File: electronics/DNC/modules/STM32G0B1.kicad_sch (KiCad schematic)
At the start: 39 parts

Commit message: Se reemplazó la hoja del IMU por la de sensores y se agregó la hoja de indicadores
- Nueva hoja Sensores: IMU BMI270 (SPI1) y barómetro BMP581 (I2C1 propio, jumper BARO_ADDR).
- Nueva hoja Indicadores: buzzer piezo CPT-12123 con FDV303N y LEDs de estado en PB4/PB5.
- Se eliminó la hoja IMU.
- MicroSD por SDIO de 4 bits con filtro TPD6F002 y TVS ESD5Z3.3 en VDD.
- PMS: AP2112K en 3V3_SYS y LP5907 + ferrita en 3V3_SEN.
- Motores movidos a PA0-PA3 (TIM5) para liberar el SDIO.
- Arquitectura.drawio actualizado a la arquitectura v1 (ELRS por UART, sin OLED).
- Se agregó docs/RESUMEN_PROYECTO_DNC.md con decisiones y pendientes.

Co-Authored-By: Claude Opus 5.5 <noreply@anthropic.com>
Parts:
- U? (x2): Category Integrated Circuits (ICs) -> (none); DK_Datasheet_Link http://www.ti.com/general/docs/suppproductinfo.tsp?distId=1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 -> (none); DK_Detail_Page /product-detail/en/texas-instruments/LM358DR/296-1014-1-ND/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 -> (none); Digi-Key_PN 296-1014-1-ND -> (none); Family Linear - Amplifiers - Instrumentation, OP Amps, Buffer Amps -> (none); MPN LM358DR -> (none); Status Active -> (none)
- U?: PROVIDER Digikey -> (none); Price 5.31 -> (none)
- U?: Category Integrated Circuits (ICs) -> (none); DK_Datasheet_Link http://www.microchip.com/mymicrochip/filehandler.aspx?ddocn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 -> (none); DK_Detail_Page /product-detail/en/microchip-technology/ATMEGA328P-AU/ATMEG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 -> (none); Digi-Key_PN ATMEGA328P-AU-ND -> (none); Family Embedded - Microcontrollers -> (none); MPN ATMEGA328P-AU -> (none); Status Active -> (none)

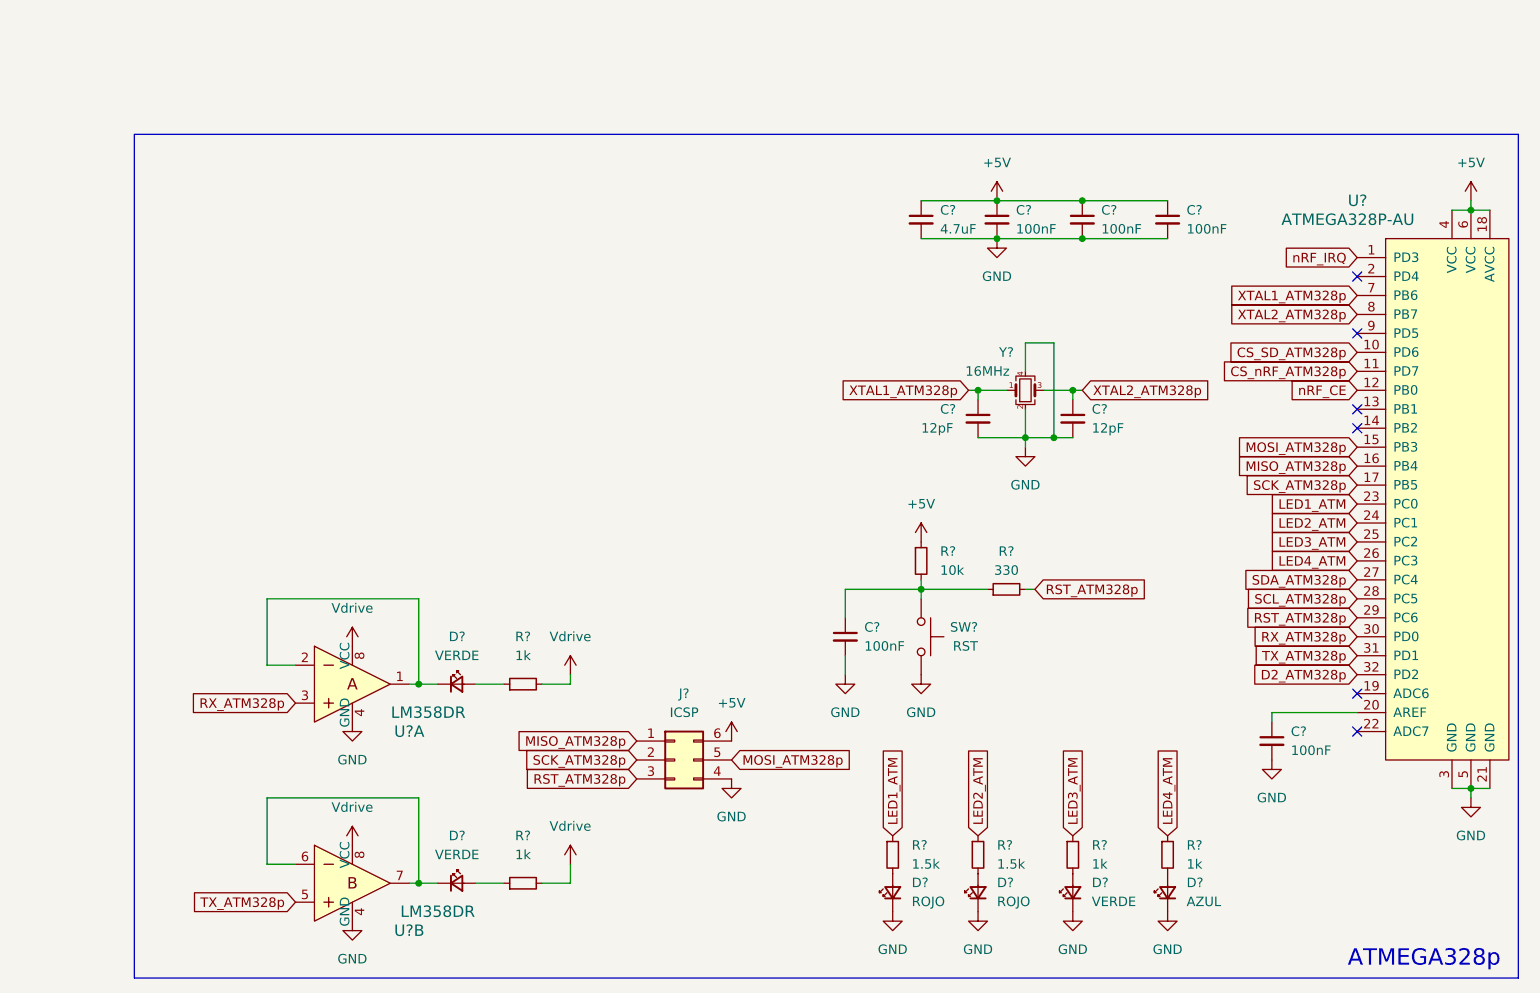
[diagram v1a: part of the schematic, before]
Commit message: Limpieza de la hoja STM32G0B1
Se eliminaron los restos del diseño anterior: ATmega328P, conector ICSP, pulsador de reset y
su cristal, LM358 y LEDs de TX/RX (alimentados desde VBUS), y los símbolos +5V y Vdrive.
La hoja ya no depende de las librerías dk_* / digikey. Quedan el STM32G0B1RETx (todavía sin
conectar) y sus dos osciladores (8 MHz y 32.768 kHz) con resistencias de 0 ohm en serie.

Co-Authored-By: Claude Opus 5.5 <noreply@anthropic.com>
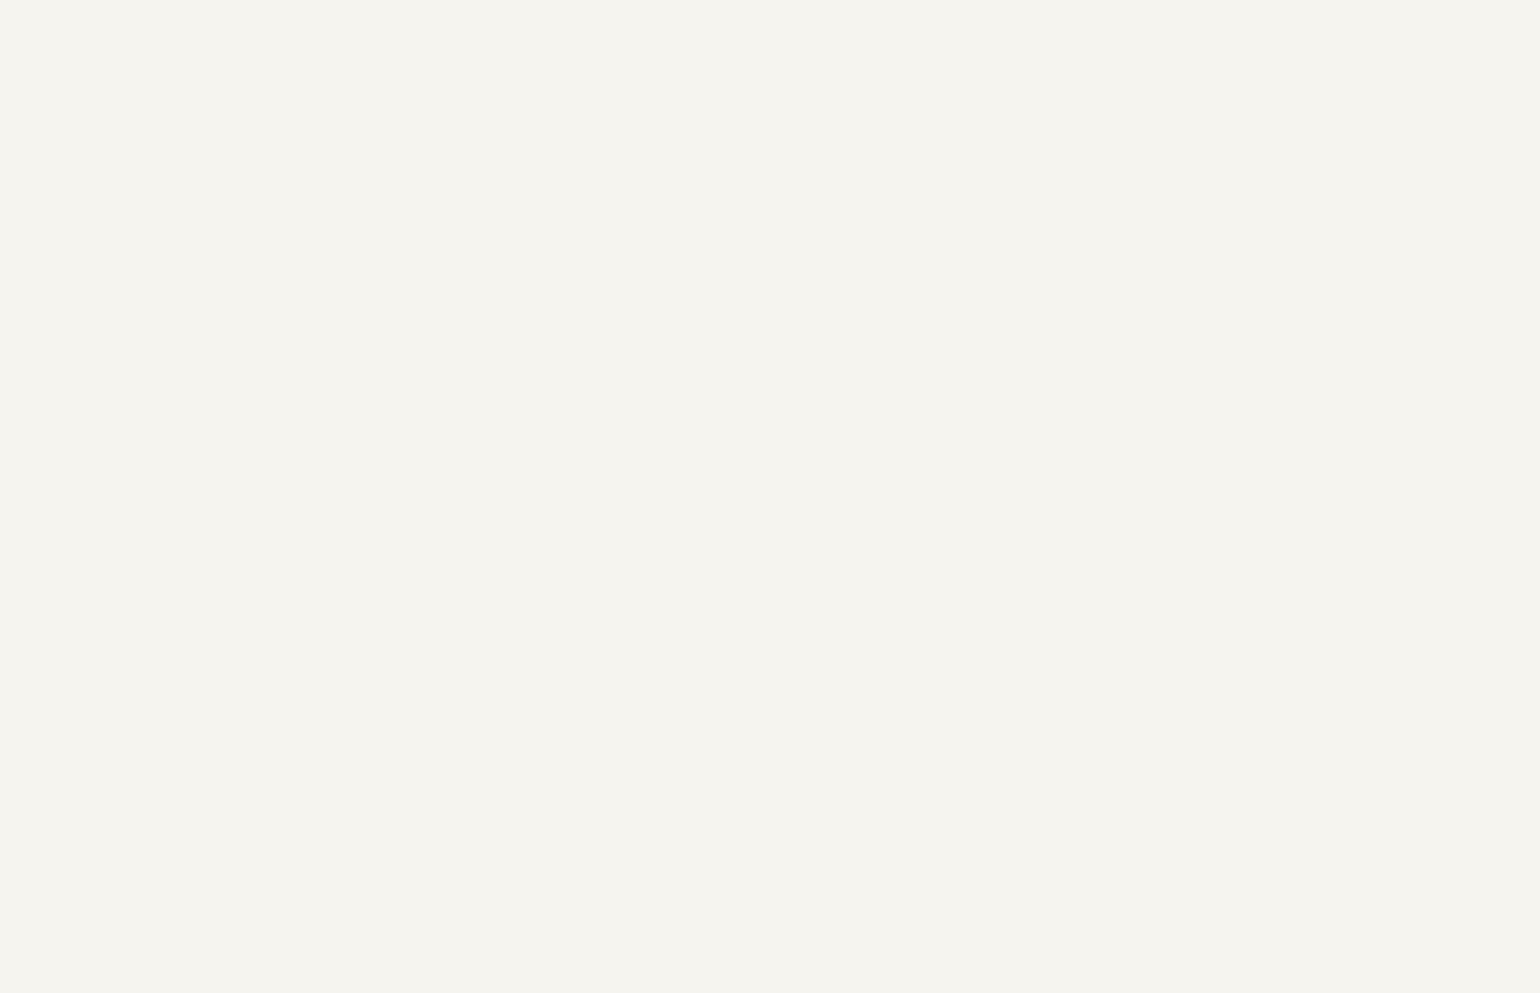
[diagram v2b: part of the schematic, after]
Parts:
- removed C? (x5): 100nF, Capacitor_SMD:C_0402_1005Metric, symbol Device:C_Small
- removed C? (x2): 12pF, Capacitor_SMD:C_0402_1005Metric, symbol Device:C_Small
- removed C?: 4.7uF, Capacitor_SMD:C_0402_1005Metric, symbol Device:C_Small
- removed D?: AZUL, LED_SMD:LED_0603_1608Metric, symbol Device:LED_Small
- removed D? (x3): VERDE, LED_SMD:LED_0603_1608Metric, symbol Device:LED_Small
- removed D? (x2): ROJO, LED_SMD:LED_0603_1608Metric, symbol Device:LED_Small
- removed J?: ICSP, Connector_PinHeader_2.54mm:PinHeader_2x03_P2.54mm_Vertical, symbol Connector_Generic:Conn_02x03_Counter_Clockwise
- removed R?: 330, Resistor_SMD:R_0402_1005Metric, symbol Device:R_Small
- removed R?: 10k, Resistor_SMD:R_0402_1005Metric, symbol Device:R_Small
- removed R? (x4): 1k, Resistor_SMD:R_0603_1608Metric, symbol Device:R_Small
- removed R? (x2): 1.5k, Resistor_SMD:R_0603_1608Metric, symbol Device:R_Small
- removed SW?: RST, Gen_devices:KEY-TH_2P-L6.0-W3.5-P6.50, symbol Switch:SW_Push
- removed U? (x2): LM358DR, digikey-footprints:SOIC-8_W3.9mm, symbol dk_Linear-Amplifiers-Instrumentation-OP-Amps-Buffer-Amps:LM358DR
- removed U?: ATMEGA328P-AU, digikey-footprints:TQFP-32_7x7mm, symbol dk_Embedded-Microcontrollers:ATMEGA328P-AU
- removed Y?: 16MHz, Crystal:Crystal_SMD_3225-4Pin_3.2x2.5mm, symbol Device:Crystal_GND24_Small
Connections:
- no-connect marks 6 -> 0
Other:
- note removed: "ATMEGA328p"
